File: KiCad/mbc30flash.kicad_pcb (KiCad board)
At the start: 2 copper layers, 51 x 60.2 mm, 19 parts, among them U0 CartBus, U1 BA6129AF, U2 74LVC1G332GW,125, X1 Crystal

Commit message: Updated to work with regular GBC shells. Also made it look a little more like an authentic cart by adding the golden squares and rounded test points in the back.
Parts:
- added  : GBA-ProductionIndicator, Custom:GBA-ProductionIndicator, F.Cu at (111.9, 110.0)
- added ?: , , F.Cu at (68.6, 94.0)
- added ?: , , F.Cu at (68.6, 88.9)
- added ?: , , F.Cu at (68.6, 104.1)
- added ?: , , F.Cu at (68.6, 99.1)
- added GNDPAD1: Nintendo_3x3_GNDPad, Custom:Nintendo_3x3_GNDPad, F.Cu at (113.2, 75.2)
- moved C2 6.20 mm to (95.8, 110.3)
- moved R2 5.10 mm to (89.6, 103.6), turned to 0 degrees
- moved C7 1.31 mm to (86.6, 91.4)
- moved U2 0.90 mm to (95.2, 91.2)
- renumbered B1 to CR2025
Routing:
- net Net-(B1-Pad1): track 28.0 -> 73.0 mm, vias 2 -> 3
- net Net-(R3-Pad2): track 3.25 -> 37.8 mm, vias 0 -> 1
- net A11: track 39.6 -> 73.9 mm, vias 0 -> 4
- net D6: track 74.8 -> 99.1 mm
- net D3: track 71.9 -> 92.6 mm
- net D7: track 78.4 -> 98.5 mm
- net D4: track 71.1 -> 90.8 mm
- net D5: track 72.7 -> 92.2 mm
- net D0: track 61.3 -> 78.5 mm
- net D1: track 64.5 -> 81.5 mm
- net D2: track 68.5 -> 83.9 mm
- net A12: track 77.9 -> 93.2 mm
- net A14: track 67.1 -> 79.1 mm
- net VCC: track 130.9 -> 140.6 mm
- net PWR: track 27.8 -> 37.2 mm, vias 0 -> 1
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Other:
- outline, holes or cut-outs redrawn
- net class Default removed
- board text added: "+"
- board text added: "-"
- board text added: "1 VDD"
- board text added: "MBC30-Flash-01"
- board text removed: "MBC30 REV 1.4.2"
- board text removed: "github.com/HDR"

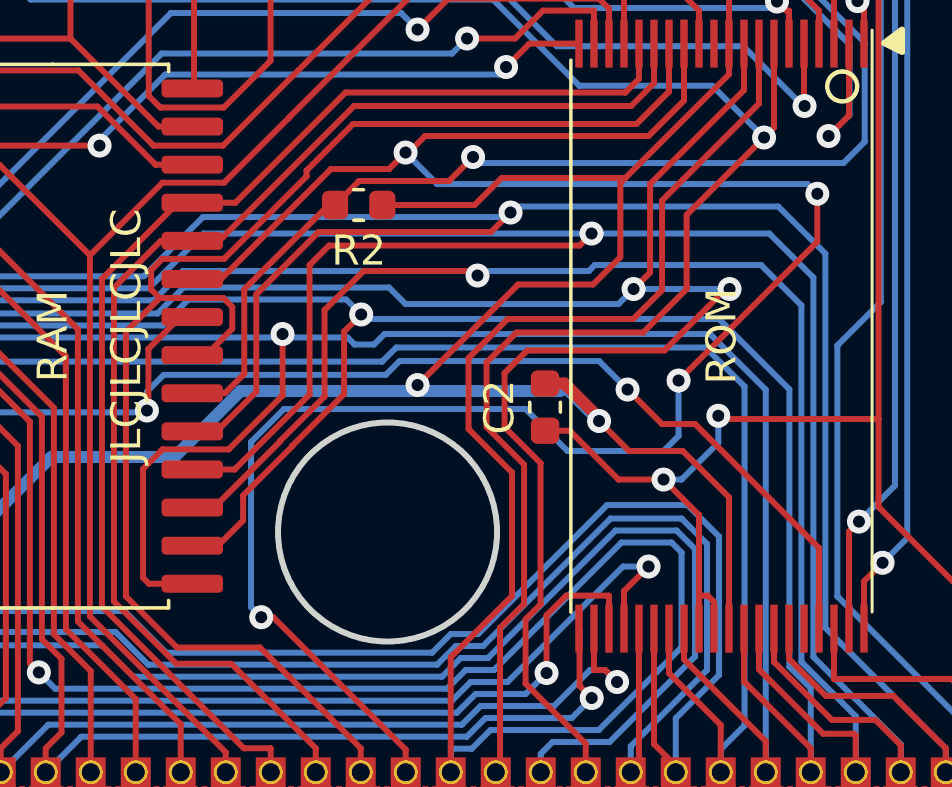
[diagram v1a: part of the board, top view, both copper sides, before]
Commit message: changed cap location
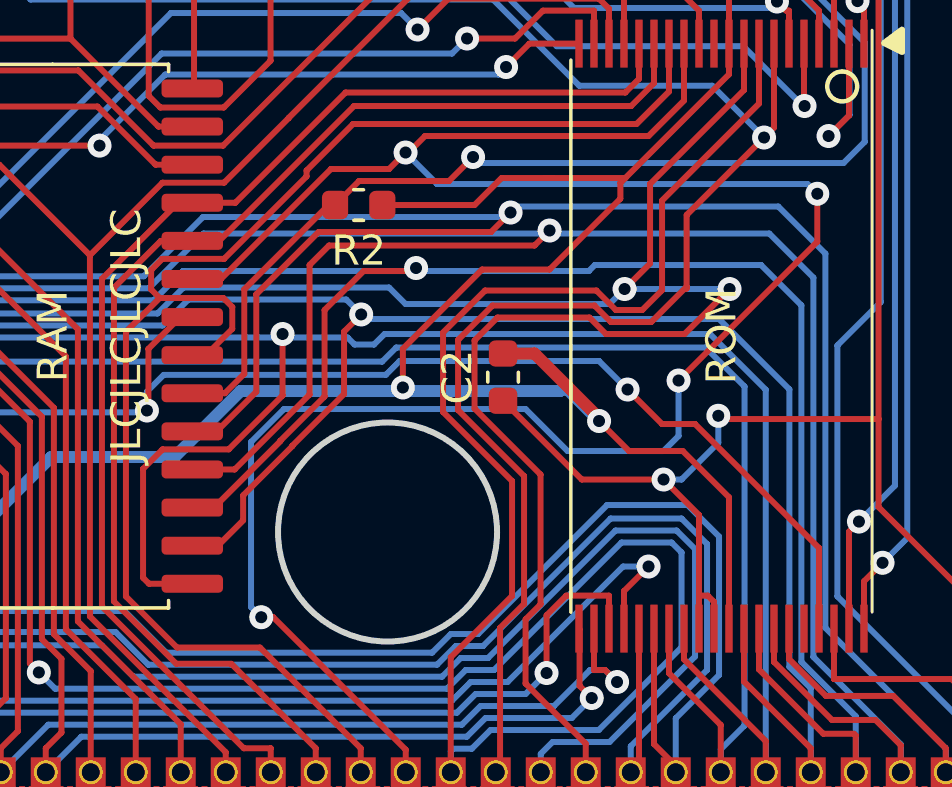
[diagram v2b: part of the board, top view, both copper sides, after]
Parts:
- moved C2 1.72 mm to (94.4, 109.3)
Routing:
- net A15: track 85.6 -> 88.2 mm
- net A12: track 93.2 -> 95.4 mm
- net A13: track 73.3 -> 75.4 mm
- net D5: track 92.2 -> 90.1 mm
- net GND: track 217.8 -> 219.6 mm
- net VCC: track 140.6 -> 142.0 mm
- net D6: track 99.1 -> 97.8 mm
